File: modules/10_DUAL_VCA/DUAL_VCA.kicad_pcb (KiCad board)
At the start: 2 copper layers, 160 x 100 mm, 33 parts, among them IC1 CA3084, IC2 µA741C, IC3 µA741C, J1 BUS CONNECTOR, P1 100k, P2 100k, P3 1k, P4 10k, T1 TUP

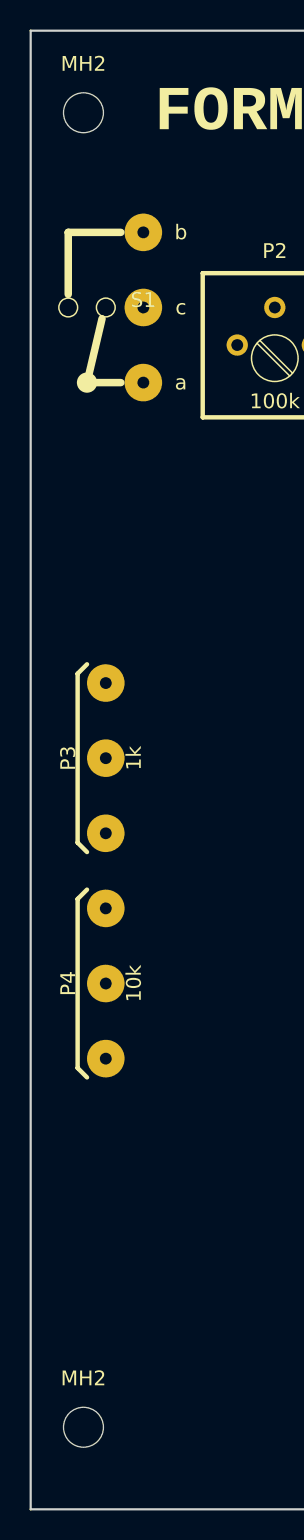
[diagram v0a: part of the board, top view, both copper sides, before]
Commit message: fixed card bracket footprint
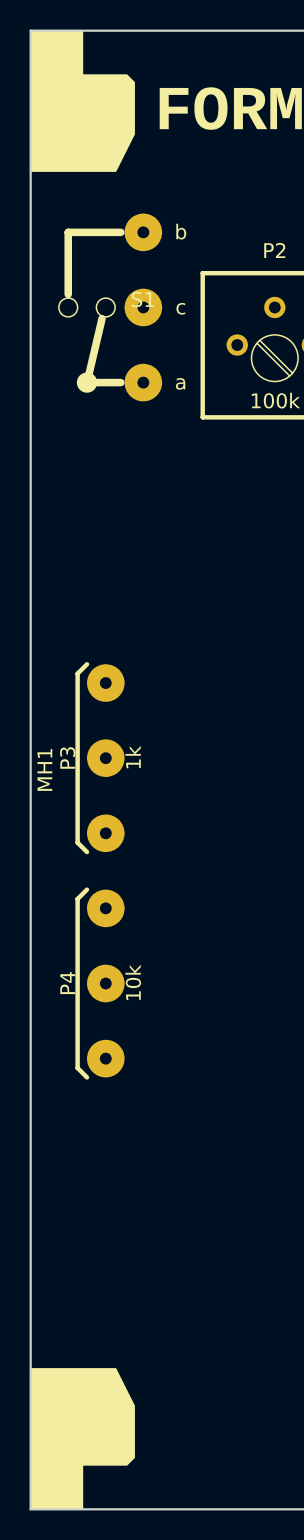
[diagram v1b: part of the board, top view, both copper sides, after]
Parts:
- removed MH2 (x2): MountingHole_2.7mm_M2.5_DIN965, MountingHole:MountingHole_2.7mm_M2.5_DIN965
- added MH1: CardBracket, FormantKO:Card_Bracket, F.Cu at (55.0, 95.0)

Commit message: vca work
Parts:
- removed MH3, MH4: MountingHole_2.7mm_M2.5_DIN965, MountingHole:MountingHole_2.7mm_M2.5_DIN965
- added C2: 680n, FormantKO:C_Disc, F.Cu at (170.0, 86.0)
- added C3: 680n, FormantKO:C_Disc, F.Cu at (115.0, 47.0)
- added D1: 1N34a, FormantKO:DUG, F.Cu at (189.0, 133.0)
- added D2: 1N34a, FormantKO:DUG, F.Cu at (197.0, 143.0)
- added D3: 1N34a, FormantKO:DUG, F.Cu at (190.0, 136.0)
- added D4: 1N34a, FormantKO:DUG, F.Cu at (180.0, 139.0)
- added D5: D_LED, FormantKO:Panel_Connector_1x02, F.Cu at (201.0, 137.0)
- added IC4: GenericOpAmp_Single, FormantKO:DIP-8, F.Cu at (81.0, 59.0)
- added IC5: GenericOpAmp_Single_Swap, FormantKO:DIP-8, F.Cu at (92.0, 59.0)
- added IC6: CA3080, FormantKO:DIP-8, F.Cu at (142.0, 79.0)
- added IC7: CA3080_Swap, FormantKO:DIP-8, F.Cu at (155.0, 120.0)
- added IC8: GenericOpAmp_Single, FormantKO:DIP-8, F.Cu at (166.0, 120.0)
- added J5: ES, FormantKO:Panel_Connector_1x02, F.Cu at (90.0, 84.0)
- added J6: ES, FormantKO:Panel_Connector_1x02, F.Cu at (169.0, 107.0)
- added J7: EOS, FormantKO:Panel_Connector_1x02, F.Cu at (167.0, 130.0)
- added P5: 100k, FormantKO:Panel_Connector_1x03, F.Cu at (172.0, 79.0)
- added P6: 4k7, FormantKO:Potentiometer_Trimmer, F.Cu at (87.0, 70.0)
- added P7: 100k, FormantKO:Potentiometer_Trimmer, F.Cu at (146.0, 131.0)
- added P8: 100k, FormantKO:Potentiometer_Trimmer, F.Cu at (144.0, 120.0)
- added R15: 100k, FormantKO:R_Axial_Horizontal, F.Cu at (112.0, 52.0)
- added R16: 100k, FormantKO:R_Axial_Horizontal, F.Cu at (112.0, 65.0)
- added R17: 33k, FormantKO:R_Axial_Horizontal, F.Cu at (74.0, 72.0)
- added R18: 100k, FormantKO:R_Axial_Horizontal, F.Cu at (102.0, 84.0)
- added R19: 12k, FormantKO:R_Axial_Horizontal, F.Cu at (117.0, 84.0)
- added R20: 100R, FormantKO:R_Axial_Horizontal, F.Cu at (144.0, 71.0)
- added R21: 3k9, FormantKO:R_Axial_Horizontal, F.Cu at (100.0, 47.0)
- added R22: 470R, FormantKO:R_Axial_Horizontal, F.Cu at (105.0, 121.0)
- added R23: 100R, FormantKO:R_Axial_Horizontal, F.Cu at (144.0, 66.0)
- added R24: 330k, FormantKO:R_Axial_Horizontal, F.Cu at (144.0, 142.0)
- added R25: 12k, FormantKO:R_Axial_Horizontal, F.Cu at (161.0, 91.0)
- added R26: 100R, FormantKO:R_Axial_Horizontal, F.Cu at (157.0, 112.0)
- added R27: 330k, FormantKO:R_Axial_Horizontal, F.Cu at (126.0, 122.0)
- added R28: 100R, FormantKO:R_Axial_Horizontal, F.Cu at (157.0, 107.0)
- added R29: 15k, FormantKO:R_Axial_Horizontal, F.Cu at (161.0, 140.0)
- added R30: 470R, FormantKO:R_Axial_Horizontal, F.Cu at (184.0, 126.0)
- D6: value DUS -> 1N4148
- J1: value BUS CONNECTOR -> CardConnector; footprint FormantKO:DIN_Male -> FormantKO:Card_Connector
- P3, P4: footprint FormantKO:Potentiometer_Inline -> FormantKO:Panel_Connector_1x03
- S1: footprint FormantKO:Switch_SPDT -> FormantKO:Panel_Connector_1x03
- T1: value TUP -> BC177C; footprint FormantKO:TUP -> FormantKO:TO-18
- moved C5 113.7 mm to (74.0, 67.0), turned to 0 degrees
- moved P4 84.9 mm to (145.0, 109.0)
- moved S1 46.7 mm to (109.0, 58.0)
- moved P2 43.1 mm to (116.0, 76.0)
- moved P3 41.3 mm to (99.0, 108.0)
- moved C4 32.7 mm to (165.0, 73.0), turned to 0 degrees
- moved R10 27.3 mm to (139.0, 56.0)
- moved R7 26.7 mm to (155.0, 66.0)
- moved R13 26.2 mm to (125.0, 105.0)
- moved C1 25.0 mm to (131.0, 86.0)
- moved D6 23.7 mm to (139.0, 138.0)
- moved R3 22.9 mm to (102.0, 89.0)
- moved C6 22.5 mm to (124.0, 135.0)
- moved J1 20.5 mm to (215.0, 95.0), turned to 0 degrees
- moved T1 18.5 mm to (175.0, 132.0)
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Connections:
- IC1 pad 1: (no net) -> unconnected-(IC1-Pad1)
- IC1 pad 11: unconnected-(IC1-C-Pad11) -> Net-(IC1-C)
- IC1 pad 12: (no net) -> unconnected-(IC1-2-Pad12)
- IC1 pad 13: (no net) -> unconnected-(IC1-2-Pad13)
- IC1 pad 14: (no net) -> unconnected-(IC1-2-Pad14)
- IC1 pad 2: (no net) -> unconnected-(IC1-Pad2)
- IC1 pad 3: (no net) -> unconnected-(IC1-Pad3)
- IC1 pad 5: (no net) -> unconnected-(IC1-Pad5)
- R1 pad 1: +15V -> Net-(S1-a)
- R1 pad 2: Net-(S1-a) -> +15V
- R10 pad 1: unconnected-(R10-Pad1) -> Net-(IC6-BIAS)
- R10 pad 2: unconnected-(R10-Pad2) -> Net-(IC1-C)
- R11 pad 1: Net-(D6-A) -> Net-(C6-Pad2)
- R11 pad 2: Net-(C6-Pad2) -> Net-(D6-A)
- R12 pad 1: Net-(D6-K) -> Net-(P4-Pad2)
- R12 pad 2: Net-(P4-Pad2) -> Net-(D6-K)
- R13 pad 1: Net-(D6-K) -> Net-(P3-Pad2)
- R13 pad 2: Net-(P3-Pad2) -> Net-(D6-K)
- R14 pad 1: +15V -> Net-(P3-Pad3)
- R14 pad 2: Net-(P3-Pad3) -> +15V
- R2 pad 1: Net-(S1-a) -> GND
- R2 pad 2: GND -> Net-(S1-a)
- R3 pad 1: Net-(IC1-B-Pad6) -> Net-(P1-Pad2)
- R3 pad 2: Net-(P1-Pad2) -> Net-(IC1-B-Pad6)
- R4 pad 1: Net-(IC1-B-Pad6) -> GND
- R4 pad 2: GND -> Net-(IC1-B-Pad6)
- R6 pad 1: Net-(IC3-+) -> GND
- R6 pad 2: GND -> Net-(IC3-+)
- R7 pad 1: Net-(IC1-E-Pad10) -> Net-(C1-Pad1)
- R7 pad 2: Net-(C1-Pad1) -> Net-(IC1-E-Pad10)
- R8 pad 1: Net-(IC3--) -> -15V
- R8 pad 2: -15V -> Net-(IC3--)
- R9 pad 1: unconnected-(R9-Pad1) -> Net-(IC7-BIAS)
- R9 pad 2: unconnected-(R9-Pad2) -> Net-(T1-C)
- T1 pad 3: unconnected-(T1-C-Pad3) -> Net-(T1-C)
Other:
- board text removed: "Mounting holes are optional Keepout areas are for for guide rails"

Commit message: lib cleanup, vca & psu work
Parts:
- added J2: ENV SELECT, Connector_PinHeader_2.54mm:PinHeader_2x04_P2.54mm_Vertical, F.Cu at (198.5, 59.4)
- added J3: IS SELECT, Connector_PinHeader_2.54mm:PinHeader_2x08_P2.54mm_Vertical, F.Cu at (198.5, 102.6)
- added J4: IOS SELECT, Connector_PinHeader_2.54mm:PinHeader_2x02_P2.54mm_Vertical, F.Cu at (198.5, 130.6)
- IC4, IC8: value GenericOpAmp_Single -> µA741C
- IC5: value GenericOpAmp_Single_Swap -> µA741C
- IC7: value CA3080_Swap -> CA3080
- J6: value ES -> AM
- S1: value ~ -> ENV
- moved D5 140.5 mm to (61.3, 121.7), turned to -90 degrees
- moved D2 123.4 mm to (74.0, 133.1)
- moved D3 116.7 mm to (74.0, 122.9), turned to 180 degrees
- moved D1 115.1 mm to (74.0, 128.0)
- moved P5 110.7 mm to (61.3, 79.8), turned to -90 degrees
- moved D4 108.0 mm to (74.0, 117.9)
- moved J6 107.8 mm to (61.3, 112.8), turned to -90 degrees
- moved C5 106.8 mm to (180.7, 62.0), turned to 90 degrees
- moved J7 105.7 mm to (61.3, 130.6), turned to -90 degrees
- moved C2 98.7 mm to (71.5, 79.8), turned to -90 degrees
- moved R21 84.1 mm to (90.5, 130.6), turned to 180 degrees
- moved P4 83.9 mm to (61.3, 102.7), turned to -90 degrees
- moved IC5 69.1 mm to (105.8, 126.8), turned to -90 degrees
- moved R29 57.0 mm to (185.8, 88.7), turned to 90 degrees
- moved P6 50.9 mm to (94.4, 120.4), turned to 180 degrees
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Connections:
- C3 pad 1: IS -> Net-(C3-Pad1)
- C3 pad 2: Net-(C3-Pad2) -> IS
- C6 pad 1: Net-(D6-K) -> Net-(C6-Pad1)
- C6 pad 2: Net-(C6-Pad2) -> Net-(D6-K)
- IC2 pad 6: Net-(C6-Pad2) -> Net-(C6-Pad1)
- R11 pad 1: Net-(C6-Pad2) -> Net-(C6-Pad1)
- R15 pad 2: Net-(C3-Pad2) -> Net-(C3-Pad1)
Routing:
- net (no net): track 0.00 -> 104.1 mm, vias 0 -> 12
- net -15V: track 0.00 -> 65.6 mm
- net Net-(D6-A): track 0.00 -> 61.0 mm
- net Net-(IC5-+): track 0.00 -> 36.1 mm, vias 0 -> 2
- net Net-(D6-K): track 0.00 -> 30.6 mm
- net Net-(T1-C): track 0.00 -> 27.9 mm
- net Net-(IC4--): track 0.00 -> 25.4 mm
- net Net-(IC5--): track 0.00 -> 20.5 mm
- net Net-(D2-A): track 0.00 -> 20.3 mm
- net Net-(C6-Pad1): track 0.00 -> 17.8 mm
- net Net-(IC5-Pad6): track 0.00 -> 17.8 mm
- net Net-(D1-K): track 0.00 -> 15.2 mm
- net Net-(D1-A): track 0.00 -> 15.2 mm
- net GND: track 0.00 -> 5.08 mm
